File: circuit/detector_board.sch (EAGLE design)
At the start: 10 parts

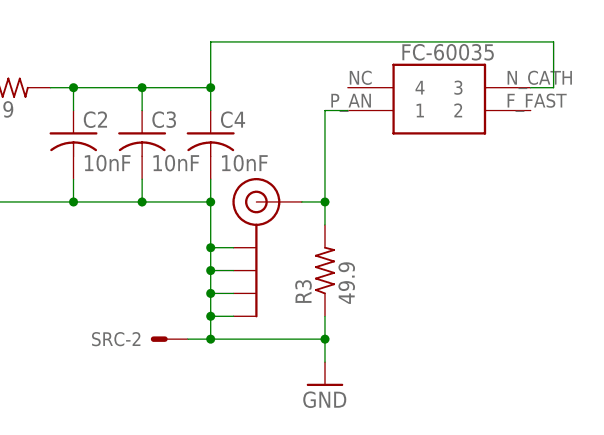
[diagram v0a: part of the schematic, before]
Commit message: boards; docs: Updated docs with impedance calculator; updated board design to stack, be solderable, and use new package design for FC-600XX.
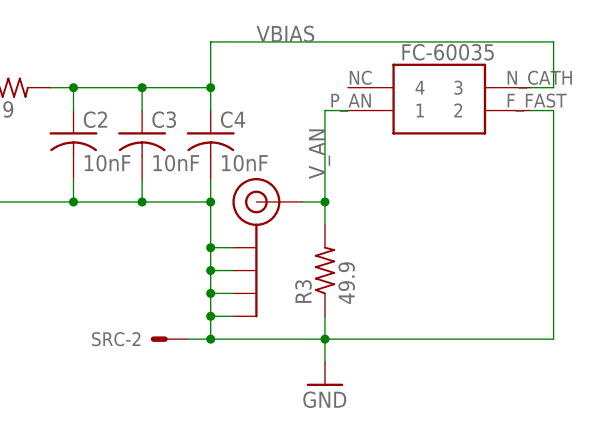
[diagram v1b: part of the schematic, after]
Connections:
- net N$2 renamed VBIAS
- net N$3 renamed V_AN
- net GND: now also FC-60035.2
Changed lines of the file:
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@@
 <?xml version="1.0" encoding="utf-8"?>
 <!DOCTYPE eagle SYSTEM "eagle.dtd">
-<eagle version="8.7.1">
+<eagle version="9.0.0">
 <drawing>
 <settings>
@@
 </variantdefs>
 <classes>
-<class number="0" name="default" width="0" drill="0">
+<class number="0" name="default" width="0.3048" drill="0">
+<clearance class="0" value="0.3048"/>
+</class>
+<class number="1" name="high_freq" width="0.184303125" drill="0">
+<clearance class="0" value="0.508"/>
+<clearance class="1" value="0.508"/>
 </class>
 </classes>
@@
 <instance part="SRC" gate="-1" x="-48.26" y="-5.08" rot="R180"/>
 <instance part="SRC" gate="-2" x="-5.08" y="-33.02" rot="R180"/>
-<instance part="FC-60035" gate="G$1" x="22.86" y="-5.08" smashed="yes">
+<instance part="FC-60035" gate="FC-60035" x="22.86" y="-5.08" smashed="yes">
 <attribute name="NAME" x="21.082" y="-2.032" size="1.778" layer="95"/>
 </instance>
@@
 </segment>
 </net>
-<net name="N$2" class="0">
+<net name="VBIAS" class="0">
 <segment>
 <pinref part="R2" gate="G$1" pin="2"/>
@@
 <wire x1="38.1" y1="0" x2="38.1" y2="-5.08" width="0.1524" layer="91"/>
 <wire x1="38.1" y1="-5.08" x2="35.56" y2="-5.08" width="0.1524" layer="91"/>
-<pinref part="FC-60035" gate="G$1" pin="3"/>
+<label x="5.08" y="0" size="1.778" layer="95"/>
+<pinref part="FC-60035" gate="FC-60035" pin="3"/>
 </segment>
 </net>
@@
 <wire x1="-2.54" y1="-33.02" x2="0" y2="-33.02" width="0.1524" layer="91"/>
 <junction x="0" y="-33.02"/>
+<wire x1="12.7" y1="-33.02" x2="38.1" y2="-33.02" width="0.1524" layer="91"/>
+<wire x1="38.1" y1="-33.02" x2="38.1" y2="-7.62" width="0.1524" layer="91"/>
+<pinref part="FC-60035" gate="FC-60035" pin="2"/>
+<wire x1="38.1" y1="-7.62" x2="35.56" y2="-7.62" width="0.1524" layer="91"/>
 </segment>
 </net>
-<net name="N$3" class="0">
+<net name="V_AN" class="1">
 <segment>
 <pinref part="R3" gate="G$1" pin="2"/>
@@
 <wire x1="10.16" y1="-17.78" x2="12.7" y2="-17.78" width="0.1524" layer="91"/>
 <junction x="12.7" y="-17.78"/>
-<pinref part="FC-60035" gate="G$1" pin="1"/>
+<label x="12.7" y="-15.24" size="1.778" layer="95" rot="R90"/>
+<pinref part="FC-60035" gate="FC-60035" pin="1"/>
 </segment>
 </net>

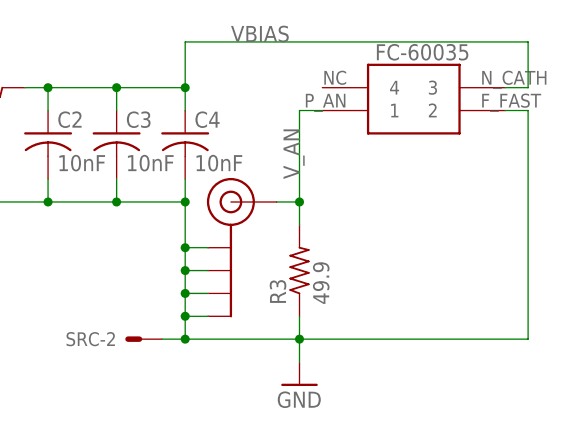
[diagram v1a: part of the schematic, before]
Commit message: boards: Changes to library and board designs.
Will I need to remove the vias and replace them with holes in order to be able to ground both sides?
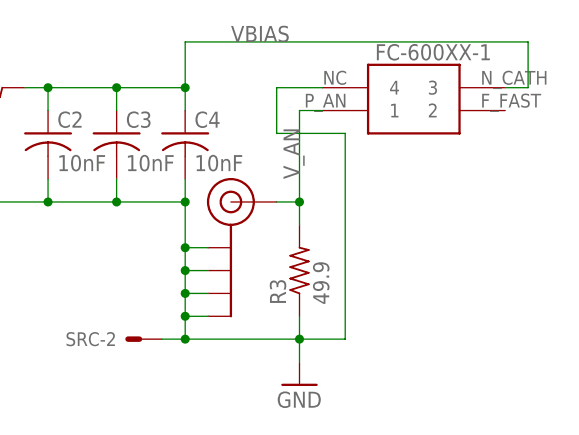
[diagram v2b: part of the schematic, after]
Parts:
- removed FC-60035: FC-600XXSMT_REFLOW, 000phys605parts:FC-600XXSMT_REFLOW
- added FC-600XX-1: FC-600XXBLANK, 000phys605parts:FC-600XXBLANK
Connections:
- net GND: now also FC-600XX-1.4; no longer FC-60035.2
- net VBIAS: now also FC-600XX-1.3; no longer FC-60035.3
- net V_AN: now also FC-600XX-1.1; no longer FC-60035.1
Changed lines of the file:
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@@
 <clearance class="0" value="0.3048"/>
 </class>
-<class number="1" name="high_freq" width="0.184303125" drill="0">
+<class number="1" name="high_freq" width="3.021" drill="0">
 <clearance class="0" value="0.508"/>
 <clearance class="1" value="0.508"/>
@@
 <part name="J$1" library="SparkFun-Retired" deviceset="SMA_EDGE" device=""/>
 <part name="SRC" library="con-garry" library_urn="urn:adsk.eagle:library:147" deviceset="332-02" device="" package3d_urn="urn:adsk.eagle:package:6810/1" value=""/>
-<part name="FC-60035" library="000phys605parts" deviceset="FC-600XX" device="" technology="SMT_REFLOW"/>
+<part name="FC-600XX-1" library="000phys605parts" deviceset="FC-600XX" device="BLANK"/>
 </parts>
 <sheets>
@@
 <instance part="SRC" gate="-1" x="-48.26" y="-5.08" rot="R180"/>
 <instance part="SRC" gate="-2" x="-5.08" y="-33.02" rot="R180"/>
-<instance part="FC-60035" gate="FC-60035" x="22.86" y="-5.08" smashed="yes">
+<instance part="FC-600XX-1" gate="FC-60035" x="22.86" y="-5.08" smashed="yes">
 <attribute name="NAME" x="21.082" y="-2.032" size="1.778" layer="95"/>
 </instance>
@@
 <wire x1="38.1" y1="-5.08" x2="35.56" y2="-5.08" width="0.1524" layer="91"/>
 <label x="5.08" y="0" size="1.778" layer="95"/>
-<pinref part="FC-60035" gate="FC-60035" pin="3"/>
+<pinref part="FC-600XX-1" gate="FC-60035" pin="3"/>
 </segment>
 </net>
@@
 <wire x1="-2.54" y1="-33.02" x2="0" y2="-33.02" width="0.1524" layer="91"/>
 <junction x="0" y="-33.02"/>
-<wire x1="12.7" y1="-33.02" x2="38.1" y2="-33.02" width="0.1524" layer="91"/>
-<wire x1="38.1" y1="-33.02" x2="38.1" y2="-7.62" width="0.1524" layer="91"/>
-<pinref part="FC-60035" gate="FC-60035" pin="2"/>
-<wire x1="38.1" y1="-7.62" x2="35.56" y2="-7.62" width="0.1524" layer="91"/>
+<wire x1="15.24" y1="-5.08" x2="10.16" y2="-5.08" width="0.1524" layer="91"/>
+<wire x1="10.16" y1="-5.08" x2="10.16" y2="-10.16" width="0.1524" layer="91"/>
+<wire x1="10.16" y1="-10.16" x2="17.78" y2="-10.16" width="0.1524" layer="91"/>
+<wire x1="17.78" y1="-10.16" x2="17.78" y2="-33.02" width="0.1524" layer="91"/>
+<wire x1="17.78" y1="-33.02" x2="12.7" y2="-33.02" width="0.1524" layer="91"/>
+<pinref part="FC-600XX-1" gate="FC-60035" pin="4"/>
 </segment>
 </net>
@@
 <junction x="12.7" y="-17.78"/>
 <label x="12.7" y="-15.24" size="1.778" layer="95" rot="R90"/>
-<pinref part="FC-60035" gate="FC-60035" pin="1"/>
+<pinref part="FC-600XX-1" gate="FC-60035" pin="1"/>
 </segment>
 </net>

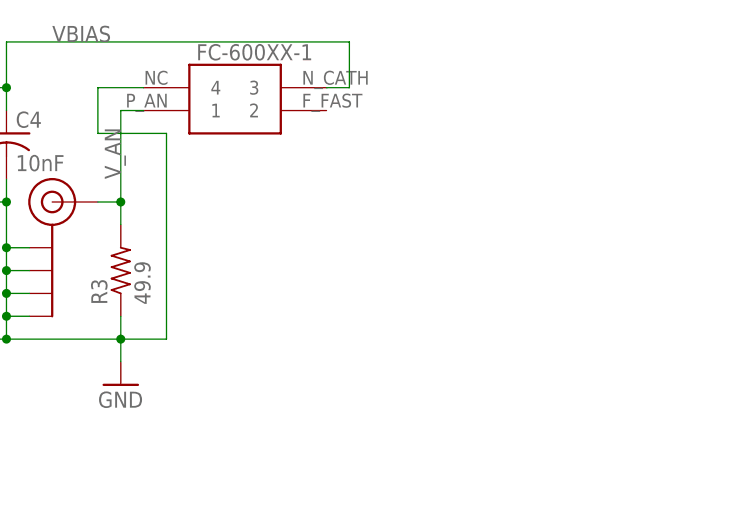
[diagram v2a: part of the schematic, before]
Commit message: boards: Changed packages of cap and resistors to be 0603, as we will have available.  Also changed mount points to be grounded, and made vias solderable.
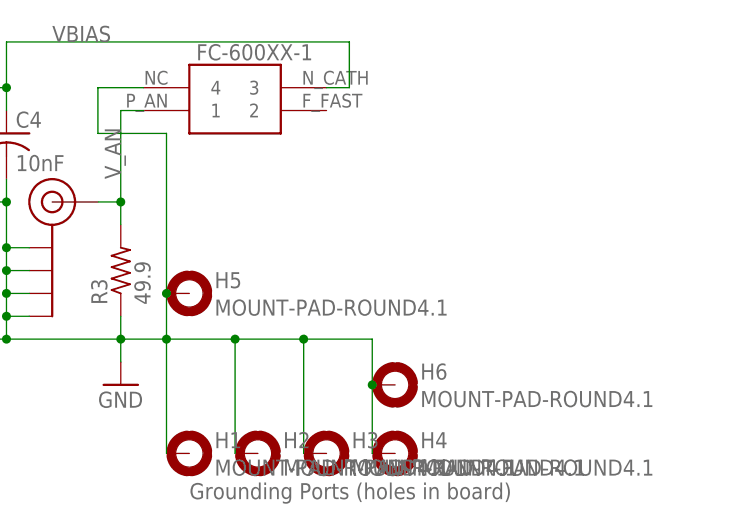
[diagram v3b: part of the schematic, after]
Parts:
- added H1, H2, H3, H4, H5, H6: MOUNT-PAD-ROUND4.1, holes:MOUNT-PAD-ROUND4.1
- C1, C2, C3, C4: device rcl:C-USC0805 -> rcl:C-USC0603
- R1, R2, R3: device rcl:R-US_R0805 -> rcl:R-US_R0603
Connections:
- net GND: now also H1.MOUNT, H2.MOUNT, H3.MOUNT, H4.MOUNT, H5.MOUNT, H6.MOUNT
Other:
- note added: "Grounding Ports (holes in board)"

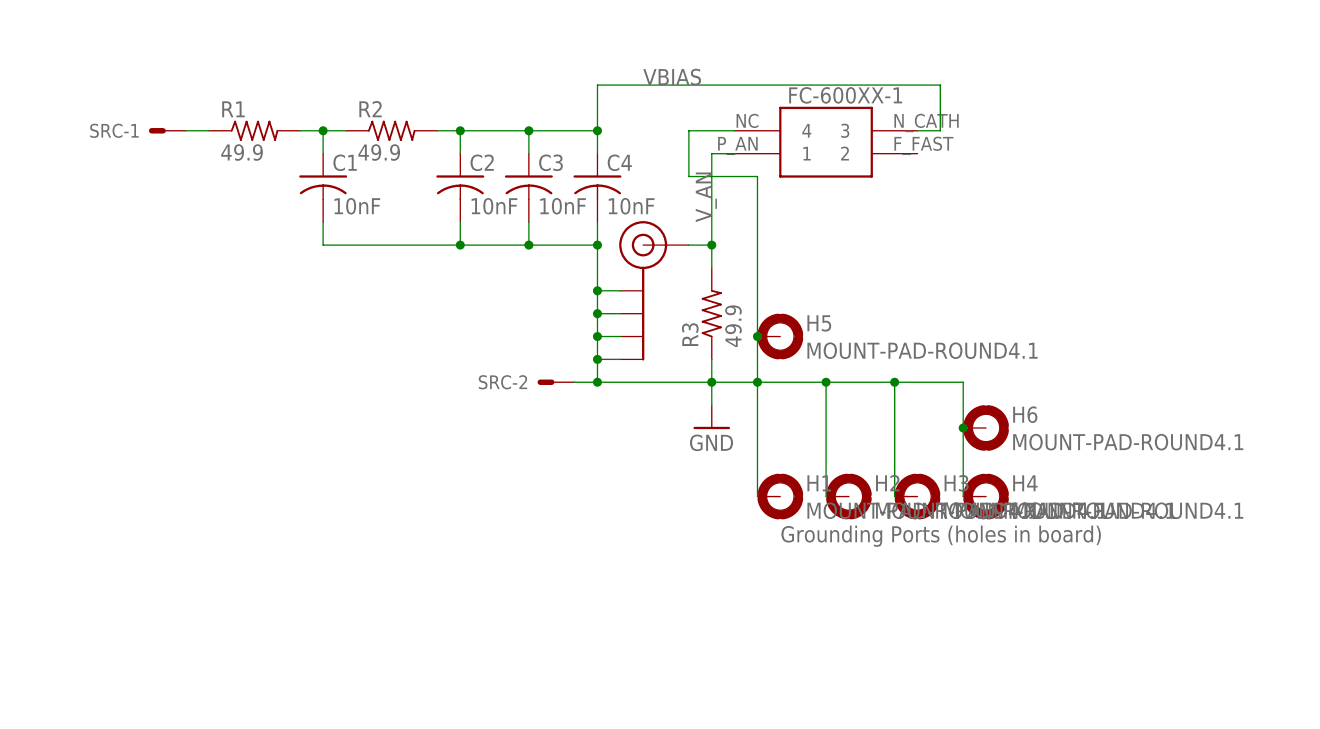
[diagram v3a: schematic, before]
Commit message: Modified board. Tried to add Spice model.
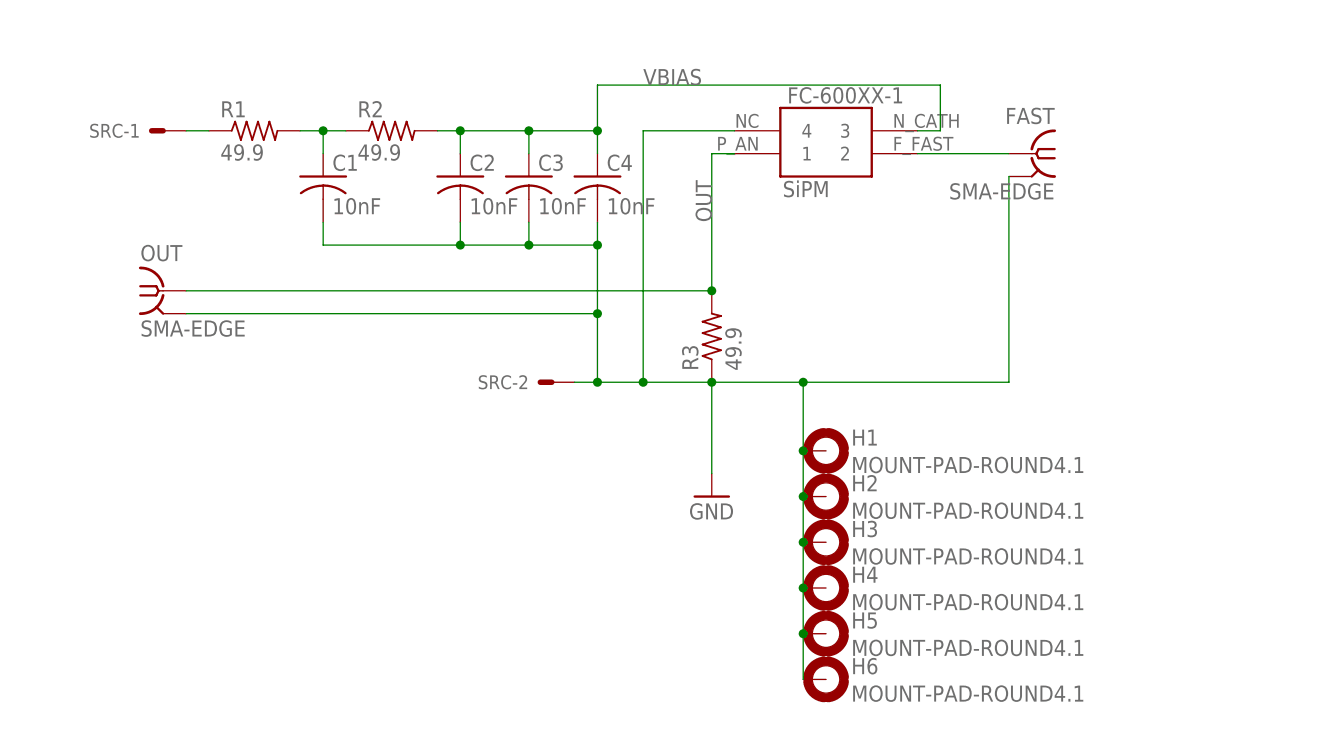
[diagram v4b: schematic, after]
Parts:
- removed J$1: SMA_EDGE, SparkFun-Retired:SMA_EDGE
- added FAST, OUT: SMA-EDGE, 000phys605parts:SMA-EDGE
- FC-600XX-1: value FC-600XXBLANK -> SiPM; device 000phys605parts:FC-600XXBLANK -> 000phys605parts:FC-600XX
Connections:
- net N$1 renamed P1
- net N$4 renamed IN
- removed net V_AN: FC-600XX-1.1, J$1.SIGNAL, R3.2
- new net FAST: FAST.1, FC-600XX-1.2
- new net OUT: FC-600XX-1.1, OUT.1, R3.2
- net GND: now also FAST.2, OUT.2; no longer J$1.GND@0, J$1.GND@1, J$1.GND@2, J$1.GND@3
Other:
- note removed: "Grounding Ports (holes in board)"
- moved on the sheet: H1, H2, H3, H4, H5, H6, R3

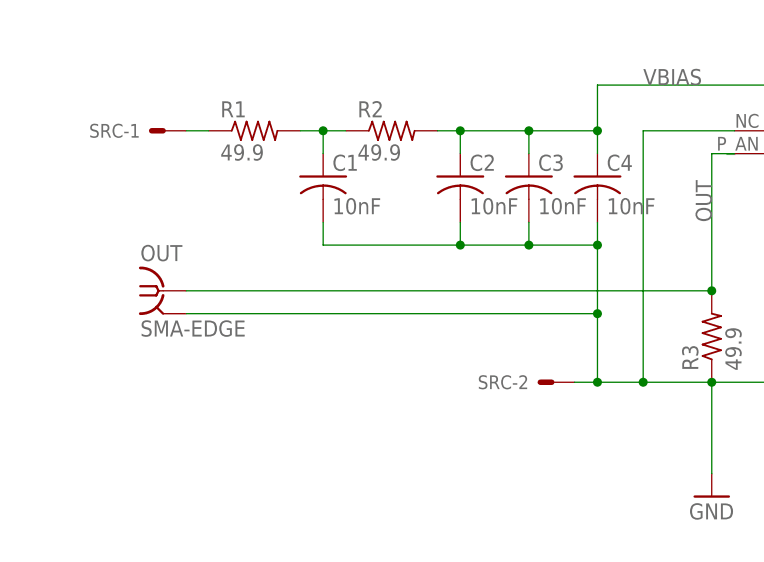
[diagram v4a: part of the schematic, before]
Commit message: boards: Added VEE line to header.  Corrected header to be 0.100", (what we have in stock,) not 2mm header.
Also added filtering caps (backwards, sort of,) to stabilize the VEE line.
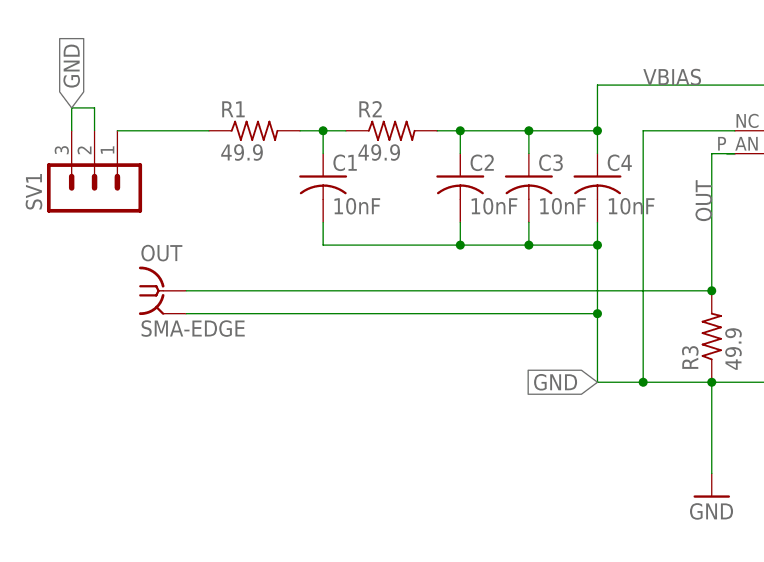
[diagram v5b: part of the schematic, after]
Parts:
- removed SRC: 332-02, con-garry:332-02
- added SV1: (no value), con-lstb:MA03-1
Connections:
- net GND: now also SV1.2, SV1.3; no longer SRC-2.S
- net IN: now also SV1.1; no longer SRC-1.S
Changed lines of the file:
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@@
 <parts>
 <part name="GND1" library="supply1" library_urn="urn:adsk.eagle:library:371" deviceset="GND" device=""/>
-<part name="SRC" library="con-garry" library_urn="urn:adsk.eagle:library:147" deviceset="332-02" device="" package3d_urn="urn:adsk.eagle:package:6810/1" value=""/>
 <part name="OUT" library="000phys605parts" deviceset="SMA-EDGE" device="">
 <attribute name="SPICEPREFIX" value="B"/>
@@
 <part name="H5" library="holes" library_urn="urn:adsk.eagle:library:237" deviceset="MOUNT-PAD-ROUND" device="4.1" package3d_urn="urn:adsk.eagle:package:14285/1"/>
 <part name="H6" library="holes" library_urn="urn:adsk.eagle:library:237" deviceset="MOUNT-PAD-ROUND" device="4.1" package3d_urn="urn:adsk.eagle:package:14285/1"/>
+<part name="SV1" library="con-lstb" library_urn="urn:adsk.eagle:library:162" deviceset="MA03-1" device="" package3d_urn="urn:adsk.eagle:package:8339/1"/>
 </parts>
 <sheets>
@@
 <instances>
 <instance part="GND1" gate="1" x="12.7" y="-45.72"/>
-<instance part="SRC" gate="-1" x="-48.26" y="-5.08" rot="R180"/>
-<instance part="SRC" gate="-2" x="-5.08" y="-33.02" rot="R180"/>
 <instance part="OUT" gate="G$1" x="-48.26" y="-22.86"/>
 <instance part="FAST" gate="G$1" x="48.26" y="-7.62" rot="MR0"/>
@@
 <instance part="H5" gate="G$1" x="25.4" y="-60.96"/>
 <instance part="H6" gate="G$1" x="25.4" y="-66.04"/>
+<instance part="SV1" gate="G$1" x="-55.88" y="-12.7" rot="R90"/>
 </instances>
 <busses>
@@
 <wire x1="0" y1="-33.02" x2="5.08" y2="-33.02" width="0.1524" layer="91"/>
 <junction x="12.7" y="-33.02"/>
-<pinref part="SRC" gate="-2" pin="S"/>
-<wire x1="-2.54" y1="-33.02" x2="0" y2="-33.02" width="0.1524" layer="91"/>
-<junction x="0" y="-33.02"/>
 <wire x1="15.24" y1="-5.08" x2="5.08" y2="-5.08" width="0.1524" layer="91"/>
 <wire x1="5.08" y1="-5.08" x2="5.08" y2="-33.02" width="0.1524" layer="91"/>
@@
 <junction x="22.86" y="-60.96"/>
 <junction x="22.86" y="-55.88"/>
+<label x="0" y="-33.02" size="1.778" layer="95" rot="R180" xref="yes"/>
+</segment>
+<segment>
+<pinref part="SV1" gate="G$1" pin="2"/>
+<wire x1="-55.88" y1="-5.08" x2="-55.88" y2="-2.54" width="0.1524" layer="91"/>
+<pinref part="SV1" gate="G$1" pin="3"/>
+<wire x1="-55.88" y1="-2.54" x2="-58.42" y2="-2.54" width="0.1524" layer="91"/>
+<wire x1="-58.42" y1="-2.54" x2="-58.42" y2="-5.08" width="0.1524" layer="91"/>
+<label x="-58.42" y="-2.54" size="1.778" layer="95" rot="R90" xref="yes"/>
 </segment>
 </net>
@@
 <net name="IN" class="0">
 <segment>
-<pinref part="SRC" gate="-1" pin="S"/>
-<wire x1="-45.72" y1="-5.08" x2="-43.18" y2="-5.08" width="0.1524" layer="91"/>
 <pinref part="R1" gate="G$1" pin="1"/>
+<pinref part="SV1" gate="G$1" pin="1"/>
+<wire x1="-53.34" y1="-5.08" x2="-43.18" y2="-5.08" width="0.1524" layer="91"/>
 </segment>
 </net>
